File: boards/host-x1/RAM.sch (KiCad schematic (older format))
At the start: 25 parts, among them U2 XC7A100T-1FTG256C, U4 S27KS0641, U5 S27KS0641, U6 S27KS0641, U7 S27KS0641

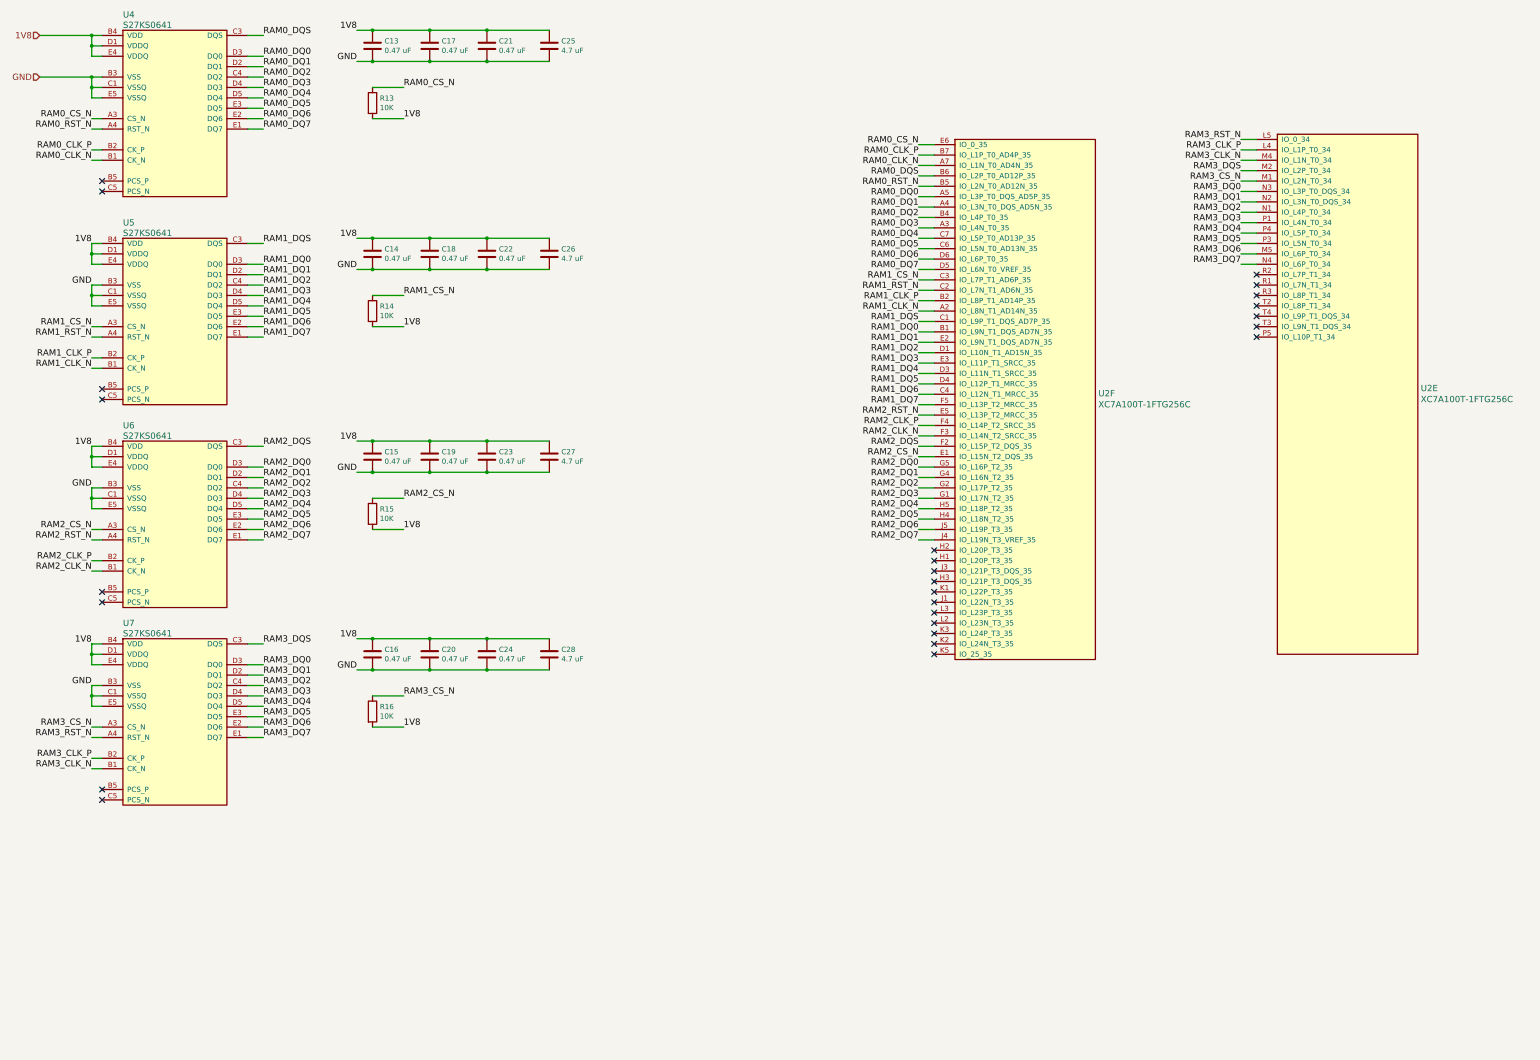
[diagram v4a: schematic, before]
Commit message: Added more test points, various tweaks for debuggability. Clarified values for design review
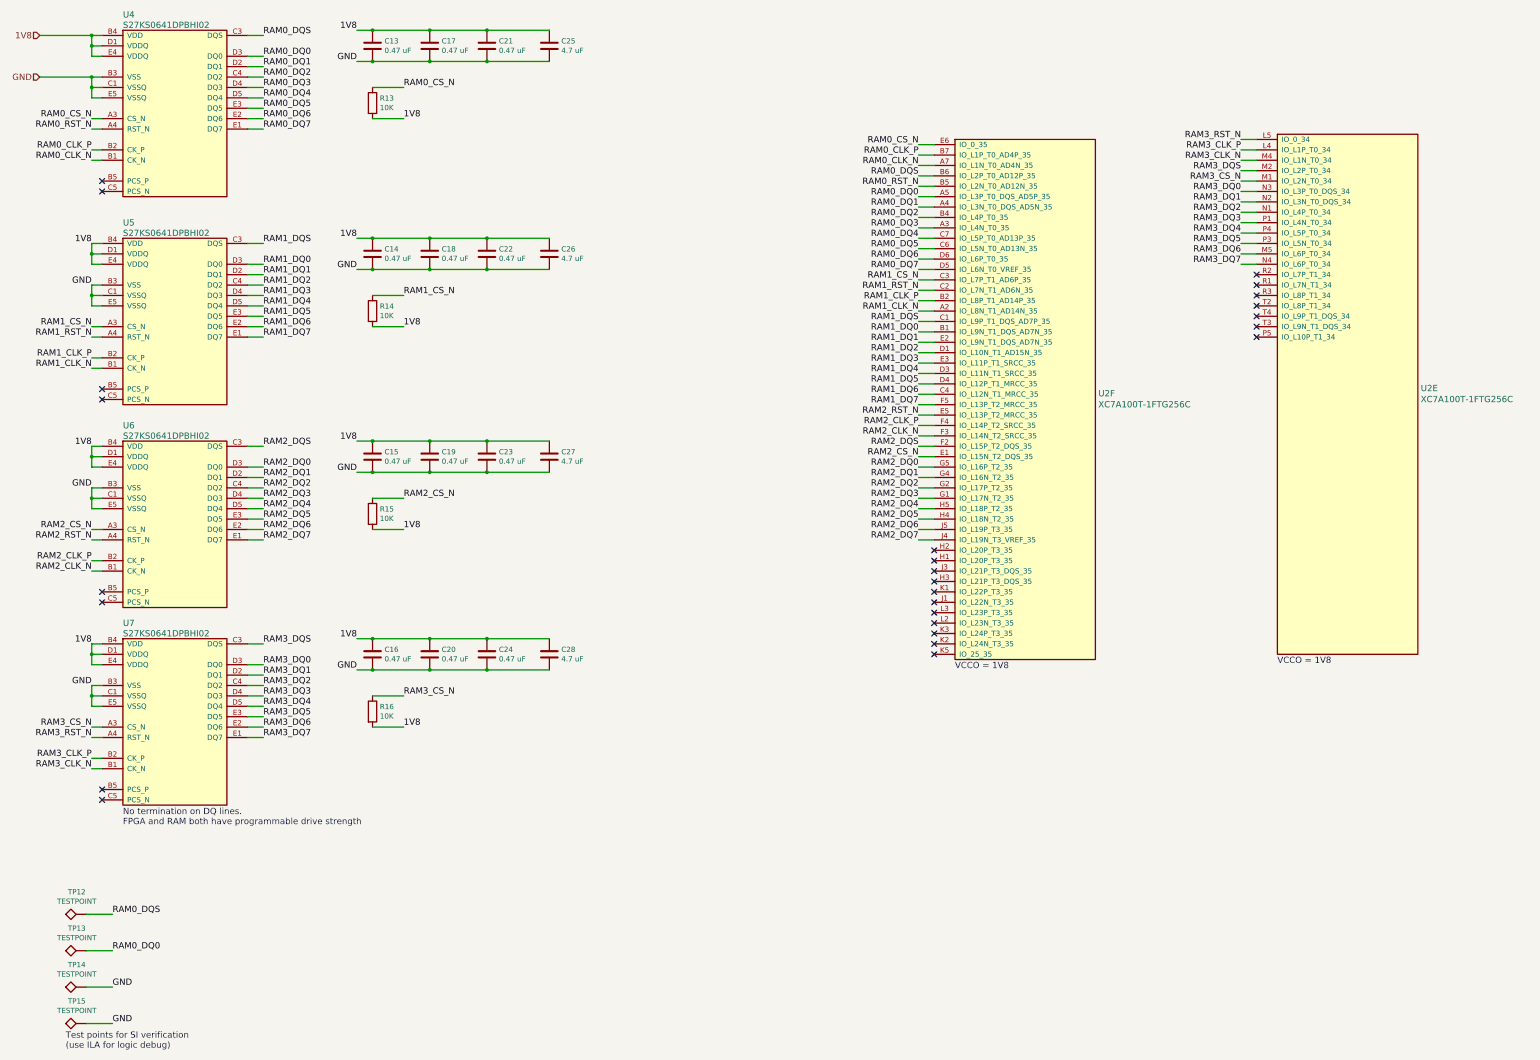
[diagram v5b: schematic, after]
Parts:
- added TP12, TP13, TP14, TP15: TESTPOINT, symbol TEST
- U4, U5, U6, U7: value S27KS0641 -> S27KS0641DPBHI02
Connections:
- net GND: now also TP14.1, TP15.1
- net RAM0_DQ0: now also TP13.1
- net RAM0_DQS: now also TP12.1
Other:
- note added: "No termination on DQ lines.\nFPGA and RAM both have programmable drive strength"
- note added: "Test points for SI verification\n(use ILA for logic debug)"
- note added: "VCCO = 1V8"
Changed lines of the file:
@@
 Sheet 3 6
 Title "STARSHIPRAIDER Single-Lane Host"
-Date "2017-05-06"
+Date "2017-05-07"
 Rev "0.1"
 Comp "Andrew D. Zonenberg"
@@
 P 2150 2750
 F 0 "U4" H 2150 4500 60  0000 L CNN
-F 1 "S27KS0641" H 2150 4400 60  0000 L CNN
+F 1 "S27KS0641DPBHI02" H 2150 4400 60  0000 L CNN
 F 2 "" H 2150 2750 60  0001 C CNN
 F 3 "" H 2150 2750 60  0001 C CNN
@@
 P 2150 4750
 F 0 "U5" H 2150 6500 60  0000 L CNN
-F 1 "S27KS0641" H 2150 6400 60  0000 L CNN
+F 1 "S27KS0641DPBHI02" H 2150 6400 60  0000 L CNN
 F 2 "" H 2150 4750 60  0001 C CNN
 F 3 "" H 2150 4750 60  0001 C CNN
@@
 P 2150 6700
 F 0 "U6" H 2150 8450 60  0000 L CNN
-F 1 "S27KS0641" H 2150 8350 60  0000 L CNN
+F 1 "S27KS0641DPBHI02" H 2150 8350 60  0000 L CNN
 F 2 "" H 2150 6700 60  0001 C CNN
 F 3 "" H 2150 6700 60  0001 C CNN
@@
 P 2150 8600
 F 0 "U7" H 2150 10350 60  0000 L CNN
-F 1 "S27KS0641" H 2150 10250 60  0000 L CNN
+F 1 "S27KS0641DPBHI02" H 2150 10250 60  0000 L CNN
 F 2 "" H 2150 8600 60  0001 C CNN
 F 3 "" H 2150 8600 60  0001 C CNN
@@
 Wire Wire Line
 	9800 5150 9950 5150
+Text Notes 10150 7300 0    60   ~ 0
+VCCO = 1V8
+Text Notes 13250 7250 0    60   ~ 0
+VCCO = 1V8
+Text Notes 2150 8800 0    60   ~ 0
+No termination on DQ lines.\nFPGA and RAM both have programmable drive strength
+$Comp
+L TEST TP12
+U 1 1 5913E5DE
+P 1800 9650
+F 0 "TP12" V 2015 9744 50  0000 C CNN
+F 1 "TESTPOINT" V 1924 9744 50  0000 C CNN
+F 2 "" H 1800 9650 50  0000 C CNN
+F 3 "" H 1800 9650 50  0000 C CNN
+	1    1800 9650
+	0    -1   -1   0
+$EndComp
+Text Label 2050 9650 0    60   ~ 0
+RAM0_DQS
+Wire Wire Line
+	2050 9650 1800 9650
+$Comp
+L TEST TP13
+U 1 1 5913E9F6
+P 1800 10000
+F 0 "TP13" V 2015 10094 50  0000 C CNN
+F 1 "TESTPOINT" V 1924 10094 50  0000 C CNN
+F 2 "" H 1800 10000 50  0000 C CNN
+F 3 "" H 1800 10000 50  0000 C CNN
+	1    1800 10000
+	0    -1   -1   0
+$EndComp
+Text Label 2050 10000 0    60   ~ 0
+RAM0_DQ0
+Wire Wire Line
+	2050 10000 1800 10000
+$Comp
+L TEST TP14
+U 1 1 5913EC17
+P 1800 10350
+F 0 "TP14" V 2015 10444 50  0000 C CNN
+F 1 "TESTPOINT" V 1924 10444 50  0000 C CNN
+F 2 "" H 1800 10350 50  0000 C CNN
+F 3 "" H 1800 10350 50  0000 C CNN
+	1    1800 10350
+	0    -1   -1   0
+$EndComp
+Text Label 2050 10350 0    60   ~ 0
+GND
+Wire Wire Line
+	2050 10350 1800 10350
+$Comp
+L TEST TP15
+U 1 1 5913ECFF
+P 1800 10700
+F 0 "TP15" V 2015 10794 50  0000 C CNN
+F 1 "TESTPOINT" V 1924 10794 50  0000 C CNN
+F 2 "" H 1800 10700 50  0000 C CNN
+F 3 "" H 1800 10700 50  0000 C CNN
+	1    1800 10700
+	0    -1   -1   0
+$EndComp
+Text Label 2050 10700 0    60   ~ 0
+GND
+Wire Wire Line
+	2050 10700 1800 10700
+Text Notes 1600 10950 0    60   ~ 0
+Test points for SI verification\n(use ILA for logic debug)
 $EndSCHEMATC
